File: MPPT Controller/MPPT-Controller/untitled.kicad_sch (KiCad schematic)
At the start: 28 parts, among them J5 USB_C_Receptacle_USB2.0_16P, U2 ESP32-WROOM-32D, U3 CH340C

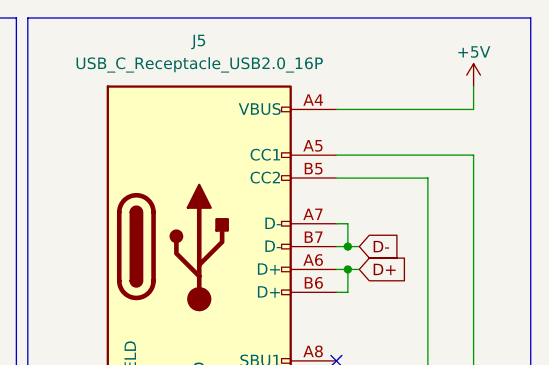
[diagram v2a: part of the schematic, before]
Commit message: Add diodes
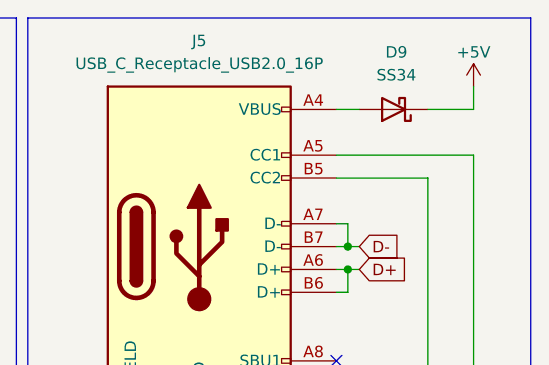
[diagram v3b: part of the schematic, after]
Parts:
- added D9: SS34, Diode_SMD:D_SMA, symbol Diode:SS34
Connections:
- net +5V: now also D9.1 (K); no longer J5.A4 (VBUS), J5.A9 (VBUS), J5.B4 (VBUS), J5.B9 (VBUS)
- new net: D9.2 (A), J5.A4 (VBUS), J5.A9 (VBUS), J5.B4 (VBUS), J5.B9 (VBUS)
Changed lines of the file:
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@@
 	(wire
 		(pts
-			(xy 154.94 22.86) (xy 170.18 22.86)
+			(xy 154.94 22.86) (xy 157.48 22.86)
 		)
 		(stroke
@@
 		)
 	)
+	(wire
+		(pts
+			(xy 165.1 22.86) (xy 170.18 22.86)
+		)
+		(stroke
+			(width 0)
+			(type default)
+		)
+	)
 	(global_label "RST"
 		(shape input)
@@
 					(unit 1)
 				)
+			)
+		)
+	)
+	(symbol
+		(lib_id "Diode:SS34")
+		(at 161.29 22.86 180)
+		(unit 1)
+		(exclude_from_sim no)
+		(in_bom yes)
+		(on_board yes)
+		(dnp no)
+		(fields_autoplaced yes)
+		(property "Reference" "D9"
+			(at 161.6075 16.51 0)
+			(effects
+				(font
+					(size 1.27 1.27)
+				)
+			)
+		)
+		(property "Value" "SS34"
+			(at 161.6075 19.05 0)
+			(effects
+				(font
+					(size 1.27 1.27)
+				)
+			)
+		)
+		(property "Footprint" "Diode_SMD:D_SMA"
+			(at 161.29 18.415 0)
+			(effects
+				(font
+					(size 1.27 1.27)
+				)
+				(hide yes)
+			)
+		)
+		(property "Datasheet" "https://www.vishay.com/docs/88751/ss32.pdf"
+			(at 161.29 22.86 0)
+			(effects
+				(font
+					(size 1.27 1.27)
+				)
+				(hide yes)
+			)
+		)
+		(property "Description" "40V 3A Schottky Diode, SMA"
+			(at 161.29 22.86 0)
+			(effects
+				(font
+					(size 1.27 1.27)
+				)
+				(hide yes)
+			)
+		)
+		(pin "2"
+		)
+		(pin "1"
+		)
+		(instances
+			(project ""
+				(path "/3478fe58-6c48-40fd-90f3-a0feb3af5722/0f80c830-9625-4e30-9255-a3bc6189ae7c"
+					(reference "D9")
+					(unit 1)
+				)
